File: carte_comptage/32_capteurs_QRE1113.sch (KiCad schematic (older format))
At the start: 96 parts, among them U1 QRE1113GR, U10 QRE1113GR, U11 QRE1113GR, U12 QRE1113GR, U13 QRE1113GR, U14 QRE1113GR, U15 QRE1113GR, U16 QRE1113GR, U17 QRE1113GR, U18 QRE1113GR, U19 QRE1113GR, U2 QRE1113GR, U20 QRE1113GR, U21 QRE1113GR, U22 QRE1113GR, U23 QRE1113GR, U24 QRE1113GR, U25 QRE1113GR, U26 QRE1113GR, U27 QRE1113GR, U28 QRE1113GR, U29 QRE1113GR, U3 QRE1113GR, U30 QRE1113GR, U31 QRE1113GR, U32 QRE1113GR, U4 QRE1113GR, U5 QRE1113GR, U6 QRE1113GR, U7 QRE1113GR, U8 QRE1113GR, U9 QRE1113GR

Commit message: Prêt à commencer le routage
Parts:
- R1, R10, R11, R12, R13, R14, R15, R16, R17, R18, R19, R2, R20, R21, R22, R23, R24, R25, R26, R27, R28, R29, R3, R30, R31, R32, R33, R34, R35, R36, R37, R38, R39, R4, R40, R41, R42, R43, R44, R45, R46, R47, R48, R49, R5, R50, R51, R52, R53, R54, R55, R56, R57, R58, R59, R6, R60, R61, R62, R63, R64, R7, R8, R9: footprint (none) -> Resistor_SMD:R_1206_3216Metric

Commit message: DEBUT ROUTAGE
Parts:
- removed R1, R41, R43, R44, R46, R48, R50, R53, R55, R57, R59, R6, R61, R63: 15, Resistor_SMD:R_1206_3216Metric, symbol Device:R
- removed R42, R45, R47, R49, R51, R52, R54, R56, R58, R60, R62, R64: 7.5k, Resistor_SMD:R_1206_3216Metric, symbol Device:R
- added R2, R3: 7.5k, Resistor_SMD:R_1206_3216Metric, symbol Device:R
- R11, R16, R2, R36: value 15 -> 42
- R13, R15, R18, R20, R22, R25, R27, R29, R30, R32, R34, R39, R4, R8: value 15 -> 7.5k
- R21, R26, R31, R5: value 7.5k -> 42
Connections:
- net GND: no longer U1.2 (K), U10.2 (K), U11.2 (K), U13.2 (K), U14.2 (K), U15.2 (K), U17.2 (K), U18.2 (K), U19.2 (K), U2.2 (K), U21.2 (K), U22.2 (K), U23.2 (K), U25.2 (K), U26.2 (K), U27.2 (K), U29.2 (K), U3.2 (K), U30.2 (K), U31.2 (K), U5.2 (K), U6.2 (K), U7.2 (K), U9.2 (K)
- net Q1: now also R2.1; no longer R5.1
- net Q10: now also R14.1; no longer R23.1
- net Q11: now also R15.1; no longer R24.1
- net Q12: now also R17.1; no longer R26.1
- net Q13: now also R18.1; no longer R28.1
- net Q14: now also R19.1; no longer R31.1
- net Q15: now also R20.1; no longer R33.1
- net Q16: now also R22.1; no longer R35.1
- net Q17: now also R23.1; no longer R37.1
- net Q18: now also R24.1; no longer R38.1
- net Q19: now also R25.1; no longer R40.1
- net Q2: now also R3.1; no longer R7.1
- net Q20: now also R27.1
- net Q21: now also R28.1
- net Q22: now also R29.1
- net Q23: now also R30.1
- net Q24: now also R32.1
- net Q25: now also R33.1
- net Q26: now also R34.1
- net Q27: now also R35.1
- net Q28: now also R37.1
- net Q29: now also R38.1
- net Q3: now also R4.1; no longer R9.1
- net Q30: now also R39.1
- net Q31: now also R40.1
- net Q4: now also R7.1; no longer R10.1
- net Q5: now also R8.1; no longer R12.1
- net Q6: now also R9.1; no longer R14.1
- net Q7: now also R10.1; no longer R17.1
- net Q8: now also R12.1; no longer R19.1
- net Q9: now also R13.1; no longer R21.1
- net Vcc: now also R13.2, R15.2, R18.2, R20.2, R22.2, R25.2, R27.2, R29.2, R30.2, R32.2, R34.2, R39.2, R4.2, R8.2, R2.2, R3.2; no longer R21.2, R26.2, R31.2, R5.2
- net Vin: now also R21.1, R26.1, R31.1, R5.1; no longer R13.1, R15.1, R18.1, R20.1, R22.1, R25.1, R27.1, R29.1, R30.1, R32.1, R34.1, R39.1, R4.1, R8.1
- net at U2.1 (A): now also U1.2 (K); no longer R4.2
- net at U3.1 (A): now also U2.2 (K)
- net at U4.1 (A): now also U3.2 (K); no longer R8.2
- net at U5.1 (A): now also R5.2
- net at U6.1 (A): now also U5.2 (K); no longer R11.2
- net at U7.1 (A): now also U6.2 (K); no longer R13.2
- net at U8.1 (A): now also U7.2 (K); no longer R16.2
- net at U9.1 (A): now also R11.2; no longer R18.2
- net at U10.1 (A): now also U9.2 (K); no longer R20.2
- net at U11.1 (A): now also U10.2 (K); no longer R22.2
- net at U12.1 (A): now also U11.2 (K); no longer R15.2
- net at U13.1 (A): now also R16.2; no longer R25.2
- net at U14.1 (A): now also U13.2 (K); no longer R27.2
- net at U15.1 (A): now also U14.2 (K); no longer R30.2
- net at U16.1 (A): now also U15.2 (K); no longer R32.2
- net at U17.1 (A): now also R21.2; no longer R34.2
- net at U18.1 (A): now also U17.2 (K); no longer R36.2
- net at U19.1 (A): now also U18.2 (K); no longer R29.2
- net at U20.1 (A): now also U19.2 (K); no longer R39.2
- net at U21.1 (A): now also R26.2
- net at U22.1 (A): now also U21.2 (K)
- net at U23.1 (A): now also U22.2 (K)
- net at U24.1 (A): now also U23.2 (K)
- net at U25.1 (A): now also R31.2
- net at U26.1 (A): now also U25.2 (K)
- net at U27.1 (A): now also U26.2 (K)
- net at U28.1 (A): now also U27.2 (K)
- net at U29.1 (A): now also R36.2
- net at U30.1 (A): now also U29.2 (K)
- net at U31.1 (A): now also U30.2 (K)
- net at U32.1 (A): now also U31.2 (K)
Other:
- note removed: "capteur QRE1113\n"
- moved on the sheet: R1, R6, U1

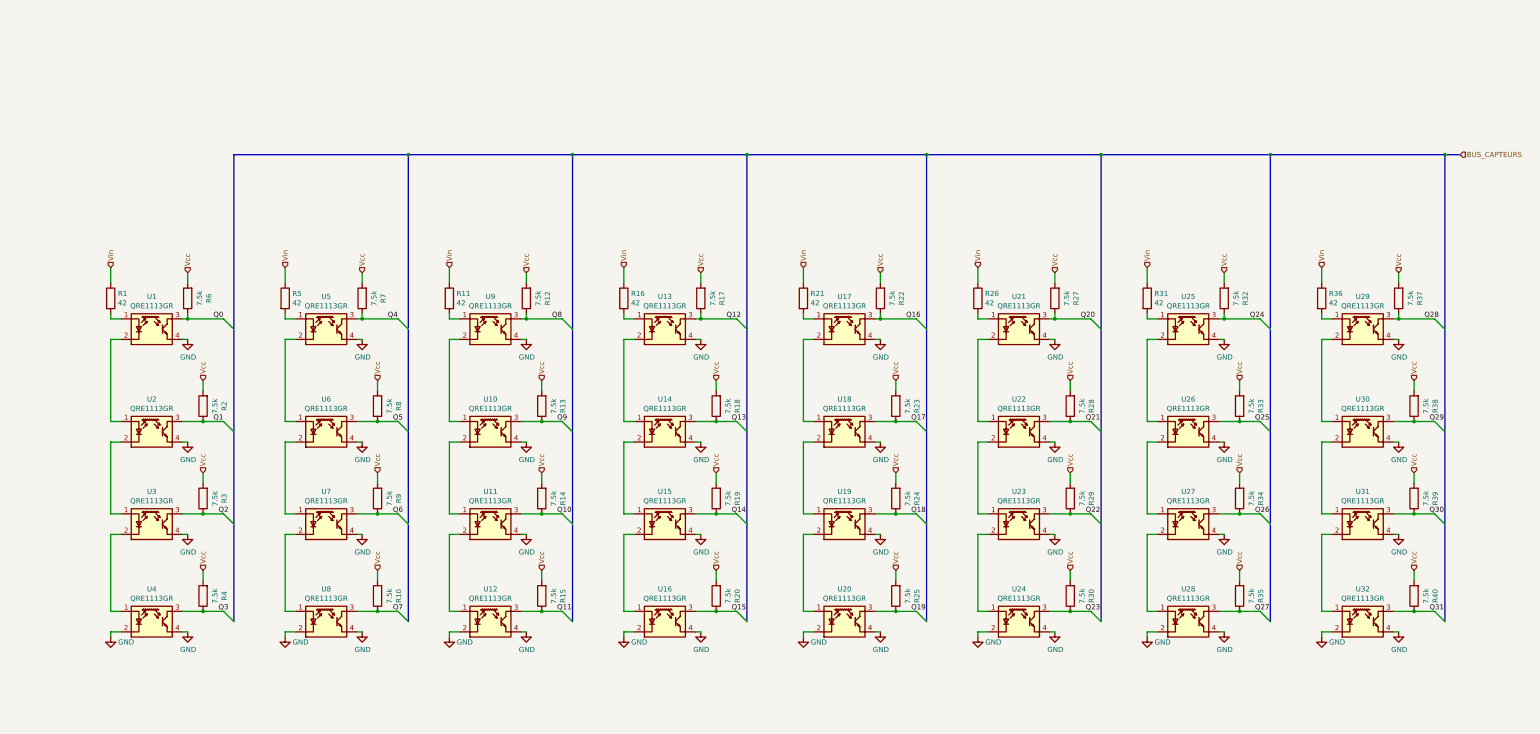
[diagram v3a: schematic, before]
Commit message: Routage fini, à vérifier, ajouter les encoches de montage
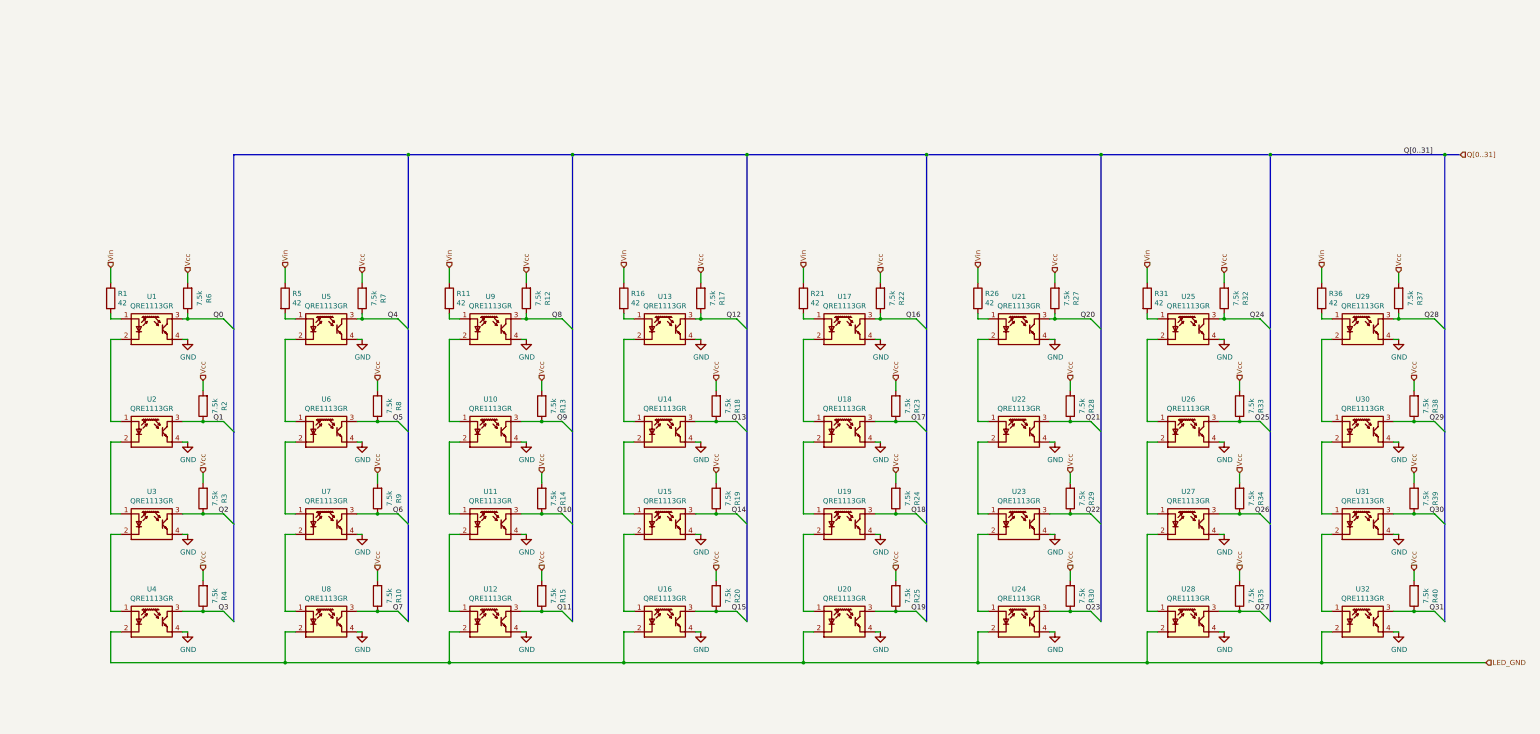
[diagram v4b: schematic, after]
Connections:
- net GND: no longer U12.2 (K), U16.2 (K), U20.2 (K), U24.2 (K), U28.2 (K), U32.2 (K), U4.2 (K), U8.2 (K)
- new net LED_GND: U12.2 (K), U16.2 (K), U20.2 (K), U24.2 (K), U28.2 (K), U32.2 (K), U4.2 (K), U8.2 (K)
